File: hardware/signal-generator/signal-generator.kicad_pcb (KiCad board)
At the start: 4 copper layers, 135 parts, among them J1 AVR-ISP-6, J10 Output_Conn, J11 SD_Card_Conn, J12 TP_Conn, J13 LCD_Conn, J2 AVR_SPI, J3 PORT_G, J4 PORT_F, J5 PORT_E, J6 PORT_A, J7 PORT_C, J8 AREF, J9 Power_Supply_Rails, Q1 AP2310GN, Q2 AP2310GN, Q3 AP2310GN, Q4 AP2310GN, Q5 AP2310GN, Q6 AP2310GN, Q7 AP2310GN, Q8 AP2310GN, Q9 AP2310GN, SW1 RESET_BUTTON, U1 74HC04, U10 MCP23017-E/SO, U11 AD9764AR, U12 TS4061AICT-1.25, U13 74HC4040, U14 74HC4040, U15 MCP4651-502E/ST, U16 AZ431AN-A, U17 AD8021ARZ, U18 MCP4551-103E/MS, U19 AD8021ARZ, U2 74HC08, U20 AD8021ARZ, U21 AD8021ARZ, U3 74HC08, U4 74HC30, U5 ATmega2561-16AU, U6 ADP7142AUJZ-5.0, U7 TC1017-3.3VCTTR, U8 DS1085Z-10+, U9 CY7C1021D-10ZSXI, Y1 16MHz

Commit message: [Signal Generator] Restore PCB layout with new symbol annotations
The new components have been loaded in the PCB file.
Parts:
- added C45: 6.8pF, Capacitors_SMD:C_0805_HandSoldering, F.Cu at (217.5, 95.6)
- added C46: 100nF, Capacitors_SMD:C_0805_HandSoldering, F.Cu at (211.9, 101.3)
- added JP2: Always_On_Backlight, Pin_Headers:Pin_Header_Straight_1x02_Pitch2.54mm, F.Cu at (45.2, 174.4)
- added Q10: AP2310GN, TO_SOT_Packages_SMD:SOT-23_Handsoldering, F.Cu at (57.2, 178.9)
- added Q11: AP2310GN, TO_SOT_Packages_SMD:SOT-23_Handsoldering, F.Cu at (43.3, 191.2)
- added Q12: AP2310GN, TO_SOT_Packages_SMD:SOT-23_Handsoldering, F.Cu at (36.8, 195.7)
- added R45: 560R, Resistors_SMD:R_0805_HandSoldering, F.Cu at (69.1, 179.3)
- added R46: 560R, Resistors_SMD:R_0805_HandSoldering, F.Cu at (65.5, 185.1)
- added R47: 1k6, Resistors_SMD:R_0805_HandSoldering, F.Cu at (65.5, 182.2)
- added R48: 1k6, Resistors_SMD:R_0805_HandSoldering, F.Cu at (55.1, 191.3)
- added R49: 1k6, Resistors_SMD:R_0805_HandSoldering, F.Cu at (55.1, 188.4)
- added R50: 1k6, Resistors_SMD:R_0805_HandSoldering, F.Cu at (48.7, 195.8)
- added R51: 910R, Resistors_SMD:R_0805_HandSoldering, F.Cu at (59.8, 185.5)
- added R52: 910R, Resistors_SMD:R_0805_HandSoldering, F.Cu at (69.1, 176.4)
- added R53: 680R, Resistors_SMD:R_0805_HandSoldering, F.Cu at (63.3, 179.3)
- added RV1: 1k, Potentiometers:Potentiometer_Alps_RK163_Single_Vertical, F.Cu at (108.6, 144.9)
- added U22: AD8021ARZ, Housings_SOIC:SOIC-8_3.9x4.9mm_Pitch1.27mm, F.Cu at (196.1, 95.3)
- C32, C35, C39: value 100nF -> 6.8pF
- C33, C37, C40, C43: value 6.8pF -> 100nF
- C34: moved to B.Cu
- JP1: value Always_On_Backlight -> MANUAL_GAIN; footprint Pin_Headers:Pin_Header_Straight_1x02_Pitch2.54mm -> Resistors_SMD:R_0805_HandSoldering
- Q1, Q2, Q3: value AP2310GN -> MMBF5485
- R10: value 15R/1% -> 10R/1%
- R11: value 10R/1% -> 510R/1%; moved to B.Cu
- R12: value 15R/1% -> 510R/1%; moved to B.Cu
- R13: value 10R/1% -> 1k/1%; moved to B.Cu
- R16: value 1k/1% -> 510R
- R17: value 2k/1% -> 1k/1%; moved to B.Cu
- R18: value 2k/1% -> 1k/1%
- R19: value 1k -> 470k
- R20: value 1k/1% -> 470k
- R21: value 2k/1% -> 100R/1%
- R22: value 1k/1% -> 100R/1%
- R23: value 1k/1% -> 2k
- R24: value 2k/1% -> 200R/1%
- R25: value 2k/1% -> 1k
- R26, R27, R28, R30: value 560R -> 1k
- R29: value 560R -> 200R/1%
- R31: value 560R -> 1k/1%
- R32: value 560R -> 680R
- R33: value 560R -> 2k4/1%
- R34: value 560R -> 100R/1%
- R38, R39, R40, R41: value 1k6 -> 560R
- R42, R43: value 910R -> 560R
- R44: value 680R -> 560R
- R7: value 1k -> 15R/1%
- R8: value 1k2 -> 10R/1%
- R9: value 2k/1% -> 15R/1%
- U15: value MCP4651-502E/ST -> MCP4551-103E/MS; footprint Housings_SSOP:TSSOP-14_4.4x5mm_Pitch0.65mm -> Housings_SSOP:MSOP-8_3x3mm_Pitch0.65mm
- U16: value AZ431AN-A -> AD8021ARZ; footprint TO_SOT_Packages_SMD:SOT-23_Handsoldering -> Housings_SOIC:SOIC-8_3.9x4.9mm_Pitch1.27mm
- U18: value MCP4551-103E/MS -> MCP4716; footprint Housings_SSOP:MSOP-8_3x3mm_Pitch0.65mm -> TO_SOT_Packages_SMD:SOT-23-6_Handsoldering
- U20: value AD8021ARZ -> MIC6211; footprint Housings_SOIC:SOIC-8_3.9x4.9mm_Pitch1.27mm -> TO_SOT_Packages_SMD:SOT-23-5_HandSoldering
- U21: value AD8021ARZ -> AZ431AN-A; footprint Housings_SOIC:SOIC-8_3.9x4.9mm_Pitch1.27mm -> TO_SOT_Packages_SMD:SOT-23_Handsoldering
- moved R33 258.7 mm to (206.3, 97.4)
- moved R32 258.3 mm to (215.5, 89.9)
- moved R30 247.1 mm to (206.3, 100.2)
- moved R29 208.6 mm to (149.0, 137.4)
- moved R34 199.3 mm to (146.0, 131.6)
- moved R2 195.0 mm to (60.4, 166.4)
- moved C1 194.8 mm to (73.3, 165.3)
- moved Q1 194.0 mm to (139.9, 132.5)
- moved U5 192.9 mm to (68.9, 139.4)
- moved Q3 191.8 mm to (131.4, 138.9)
- moved C11 191.5 mm to (76.5, 151.5)
- moved U7 190.7 mm to (67.7, 163.4)
- moved C12 190.2 mm to (68.6, 158.2)
- moved C14 190.1 mm to (88.8, 147.4)
- moved U21 189.7 mm to (203.6, 87.9)
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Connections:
- C30 pad 1: Net-(C30-Pad1) -> +5VA
- C31 pad 2: +5VA -> -12VA
- C32 pad 1: AGND -> Net-(C32-Pad1)
- C33 pad 1: Net-(C33-Pad1) -> AGND
- C35 pad 1: +5VA -> Net-(C35-Pad1)
- C35 pad 2: AGND -> -12VA
- C36 pad 1: AGND -> +12VA
- C36 pad 2: -12VA -> AGND
- C37 pad 1: Net-(C37-Pad1) -> +5VA
- C37 pad 2: -12VA -> AGND
- C39 pad 1: +12VA -> Net-(C39-Pad1)
- C39 pad 2: AGND -> -12VA
- C40 pad 1: Net-(C40-Pad1) -> AGND
- C41 pad 1: +12VA -> AGND
- C41 pad 2: AGND -> +12VA
- C42 pad 1: AGND -> +12VA
- C42 pad 2: -12VA -> AGND
- C43 pad 2: -12VA -> AGND
- C44 pad 1: +12VA -> AGND
- C44 pad 2: AGND -> -12VA
- JP1 pad 1: +3V3 -> Net-(JP1-Pad1)
- JP1 pad 2: AGND -> Net-(JP1-Pad2)
- Q1 pad 1: +3V3 -> Net-(JP1-Pad2)
- Q1 pad 2: /TFT LCD Module Interface Block/MISO_3.3 -> AGND
- Q1 pad 3: /MISO -> Net-(Q1-Pad3)
- Q2 pad 1: +3V3 -> Net-(JP1-Pad2)
- Q2 pad 2: /TFT LCD Module Interface Block/SCK_3.3 -> AGND
- Q2 pad 3: /SCK -> Net-(Q1-Pad3)
- Q3 pad 1: +3V3 -> Net-(JP1-Pad2)
- Q3 pad 2: /TFT LCD Module Interface Block/MOSI_3.3 -> AGND
- Q3 pad 3: /MOSI -> Net-(Q1-Pad3)
- Q4 pad 2: /TFT LCD Module Interface Block/LCD_DC\~RS -> /TFT LCD Module Interface Block/MISO_3.3
- Q4 pad 3: /DC\~RS~_LCD -> /MISO
- Q5 pad 2: /TFT LCD Module Interface Block/LCD_~RESET -> /TFT LCD Module Interface Block/SCK_3.3
- Q5 pad 3: /~RESET~_LCD -> /SCK
- Q6 pad 2: /TFT LCD Module Interface Block/LCD_~CS -> /TFT LCD Module Interface Block/MOSI_3.3
- Q6 pad 3: /~CS~_LCD -> /MOSI
- Q7 pad 2: /TFT LCD Module Interface Block/T_IRQ -> /TFT LCD Module Interface Block/LCD_DC\~RS
- Q7 pad 3: /IRQ_T -> /DC\~RS~_LCD
- Q8 pad 2: /TFT LCD Module Interface Block/T_~CS -> /TFT LCD Module Interface Block/LCD_~RESET
- Q8 pad 3: /~CS~_T -> /~RESET~_LCD
- Q9 pad 2: /TFT LCD Module Interface Block/SD_~CS -> /TFT LCD Module Interface Block/LCD_~CS
- Q9 pad 3: /~CS~_SD -> /~CS~_LCD
- R10 pad 1: /Output Circuitry/INB -> Net-(R10-Pad1)
- R10 pad 2: Net-(R10-Pad2) -> AGND
- R11 pad 1: Net-(R10-Pad2) -> Net-(R11-Pad1)
- R11 pad 2: AGND -> /Output Circuitry/INA
- R12 pad 1: /Output Circuitry/INA -> Net-(R12-Pad1)
- R12 pad 2: Net-(R12-Pad2) -> /Output Circuitry/INB
- R13 pad 1: Net-(R12-Pad2) -> Net-(R12-Pad1)
- R14 pad 2: /Output Circuitry/INA -> /OCAL
- R15 pad 1: Net-(R15-Pad1) -> Net-(R14-Pad1)
- R15 pad 2: /Output Circuitry/INB -> Net-(R15-Pad2)
- R16 pad 1: Net-(R15-Pad1) -> Net-(R16-Pad1)
- R17 pad 1: Net-(R17-Pad1) -> Net-(JP1-Pad1)
- R17 pad 2: /OCAL -> Net-(R11-Pad1)
- R18 pad 1: Net-(R17-Pad1) -> Net-(R18-Pad1)
- R18 pad 2: Net-(R18-Pad2) -> Net-(R14-Pad1)
- R19 pad 1: Net-(R19-Pad1) -> Net-(Q1-Pad3)
- R19 pad 2: AGND -> /Output Circuitry/GAINCTRL
- R20 pad 1: /Output Circuitry/VINamp -> Net-(JP1-Pad2)
- R20 pad 2: Net-(R14-Pad1) -> Net-(Q1-Pad3)
- R21 pad 2: Net-(R17-Pad1) -> +5VA
- R22 pad 2: +5VA -> Net-(R18-Pad1)
- R23 pad 1: Net-(R23-Pad1) -> Net-(JP1-Pad1)
- R23 pad 2: Net-(R21-Pad1) -> Net-(JP1-Pad2)
- R24 pad 2: Net-(R23-Pad1) -> Net-(R22-Pad1)
- R25 pad 1: /Output Circuitry/VOUT -> Net-(R25-Pad1)
- R25 pad 2: Net-(R22-Pad1) -> +5VA
- R26 pad 1: +5VD -> Net-(R26-Pad1)
- R26 pad 2: /MISO -> Net-(R26-Pad2)
- R27 pad 1: +5VD -> AGND
- R27 pad 2: /SCK -> Net-(R26-Pad1)
- R28 pad 1: +5VD -> /Output Circuitry/GAINCTRL
- R28 pad 2: /MOSI -> Net-(R25-Pad1)
- R29 pad 1: +3V3 -> /Output Circuitry/VOUT
- R29 pad 2: /TFT LCD Module Interface Block/MISO_3.3 -> Net-(R21-Pad1)
- R30 pad 1: +3V3 -> +5VA
- R30 pad 2: /TFT LCD Module Interface Block/SCK_3.3 -> Net-(C43-Pad1)
- R31 pad 1: +3V3 -> Net-(R31-Pad1)
- R31 pad 2: /TFT LCD Module Interface Block/MOSI_3.3 -> Net-(JP1-Pad2)
- R32 pad 1: +5VD -> Net-(R32-Pad1)
- R32 pad 2: /DC\~RS~_LCD -> Net-(C43-Pad1)
- R33 pad 1: +5VD -> Net-(R33-Pad1)
- R33 pad 2: /~RESET~_LCD -> Net-(R31-Pad1)
- R34 pad 1: +5VD -> /OCAL
- R34 pad 2: /~CS~_LCD -> Net-(R33-Pad1)
- R35 pad 1: +3V3 -> +5VD
- R35 pad 2: /TFT LCD Module Interface Block/LCD_DC\~RS -> /MISO
- R36 pad 1: +3V3 -> +5VD
- R36 pad 2: /TFT LCD Module Interface Block/LCD_~RESET -> /SCK
- R37 pad 1: +3V3 -> +5VD
- R37 pad 2: /TFT LCD Module Interface Block/LCD_~CS -> /MOSI
- R38 pad 1: +5VD -> +3V3
- R38 pad 2: /IRQ_T -> /TFT LCD Module Interface Block/MISO_3.3
- R39 pad 1: +5VD -> +3V3
- R39 pad 2: /~CS~_T -> /TFT LCD Module Interface Block/SCK_3.3
- R40 pad 2: /TFT LCD Module Interface Block/T_IRQ -> /TFT LCD Module Interface Block/MOSI_3.3
- R41 pad 1: +3V3 -> +5VD
- R41 pad 2: /TFT LCD Module Interface Block/T_~CS -> /DC\~RS~_LCD
- R42 pad 2: /~CS~_SD -> /~RESET~_LCD
- R43 pad 1: +3V3 -> +5VD
- R43 pad 2: /TFT LCD Module Interface Block/SD_~CS -> /~CS~_LCD
- R44 pad 1: AGND -> +3V3
- R44 pad 2: /BL_LCD -> /TFT LCD Module Interface Block/LCD_DC\~RS
- R7 pad 1: +5VA -> /Output Circuitry/INB
- R7 pad 2: Net-(C30-Pad1) -> Net-(R7-Pad2)
- R8 pad 1: Net-(R8-Pad1) -> Net-(R7-Pad2)
- R8 pad 2: Net-(C30-Pad1) -> AGND
- R9 pad 1: /OCAL -> /Output Circuitry/INA
- R9 pad 2: Net-(R9-Pad2) -> Net-(R10-Pad1)
- U15 pad 5: Net-(U15-Pad10) -> +5VA
- U15 pad 6: Net-(U15-Pad10) -> Net-(R15-Pad2)
- U15 pad 7: /Output Circuitry/VINamp -> AGND
- U15 pad 8: Net-(R9-Pad2) -> +5VA
- U16 pad 1: Net-(C30-Pad1) -> AGND
- U16 pad 2: Net-(C30-Pad1) -> Net-(R11-Pad1)
- U16 pad 3: AGND -> Net-(R12-Pad1)
- U17 pad 2: Net-(U15-Pad10) -> Net-(R14-Pad1)
- U17 pad 3: Net-(R8-Pad1) -> Net-(R16-Pad1)
- U17 pad 5: Net-(C33-Pad1) -> Net-(C35-Pad1)
- U17 pad 6: /OCAL -> Net-(R18-Pad1)
- U18 pad 1: AGND -> Net-(R26-Pad2)
- U18 pad 2: /SCL -> AGND
- U18 pad 3: /SDA -> +5VA
- U18 pad 4: AGND -> /SDA
- U18 pad 5: +5VA -> /SCL
- U18 pad 6: Net-(R18-Pad2) -> Net-(U18-Pad6)
- U19 pad 2: Net-(R14-Pad1) -> Net-(R21-Pad1)
- U19 pad 3: Net-(R15-Pad1) -> Net-(R22-Pad1)
- U19 pad 5: Net-(C37-Pad1) -> Net-(C39-Pad1)
- U19 pad 6: /Output Circuitry/VINamp -> /Output Circuitry/VOUT
- U2 pad 1: /DDS System/16-bit Counter/Q11 -> Net-(U2-Pad1)
- U2 pad 10: /DDS System/16-bit Counter/Q5 -> /DDS System/16-bit Counter/Q1
- U2 pad 11: /DDS System/16-bit Counter/CP2I3 -> /DDS System/16-bit Counter/CP2I1
- U2 pad 12: /DDS System/16-bit Counter/Q6 -> /DDS System/16-bit Counter/Q2
- U2 pad 13: /DDS System/16-bit Counter/Q7 -> /DDS System/16-bit Counter/Q3
- U2 pad 2: /DDS System/16-bit Counter/Q10 -> Net-(U2-Pad2)
- U2 pad 3: /DDS System/16-bit Counter/CP2I5 -> Net-(U2-Pad3)
- U2 pad 4: /DDS System/16-bit Counter/Q9 -> Net-(U2-Pad4)
- U2 pad 5: /DDS System/16-bit Counter/Q8 -> Net-(U2-Pad5)
- U2 pad 6: /DDS System/16-bit Counter/CP2I4 -> Net-(U2-Pad6)
- U2 pad 8: /DDS System/16-bit Counter/CP2I2 -> /DDS System/16-bit Counter/CP2I0
- U2 pad 9: /DDS System/16-bit Counter/Q4 -> /DDS System/16-bit Counter/Q0
- U20 pad 1: AGND -> /Output Circuitry/GAINCTRL
- U20 pad 2: Net-(R17-Pad1) -> -12VA
- U20 pad 3: Net-(R19-Pad1) -> Net-(R26-Pad1)
- U20 pad 4: -12VA -> Net-(R25-Pad1)
- U20 pad 5: Net-(C40-Pad1) -> +12VA
- U21 pad 1: AGND -> Net-(C43-Pad1)
- U21 pad 2: Net-(R22-Pad1) -> Net-(C43-Pad1)
- U21 pad 3: Net-(R23-Pad1) -> AGND
- U3 pad 1: Net-(U3-Pad1) -> /DDS System/16-bit Counter/Q11
- U3 pad 10: /DDS System/16-bit Counter/Q1 -> /DDS System/16-bit Counter/Q5
- U3 pad 11: /DDS System/16-bit Counter/CP2I1 -> /DDS System/16-bit Counter/CP2I3
- U3 pad 12: /DDS System/16-bit Counter/Q2 -> /DDS System/16-bit Counter/Q6
- U3 pad 13: /DDS System/16-bit Counter/Q3 -> /DDS System/16-bit Counter/Q7
- U3 pad 2: Net-(U3-Pad2) -> /DDS System/16-bit Counter/Q10
- U3 pad 3: Net-(U3-Pad3) -> /DDS System/16-bit Counter/CP2I5
- U3 pad 4: Net-(U3-Pad4) -> /DDS System/16-bit Counter/Q9
- U3 pad 5: Net-(U3-Pad5) -> /DDS System/16-bit Counter/Q8
- U3 pad 6: Net-(U3-Pad6) -> /DDS System/16-bit Counter/CP2I4
- U3 pad 8: /DDS System/16-bit Counter/CP2I0 -> /DDS System/16-bit Counter/CP2I2
- U3 pad 9: /DDS System/16-bit Counter/Q0 -> /DDS System/16-bit Counter/Q4
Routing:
- net AGND: track 60.8 -> 86.7 mm, vias 32 -> 45
- net Net-(R31-Pad1): track 0.00 -> 23.7 mm, vias 0 -> 3
- net Net-(JP1-Pad1): track 0.00 -> 23.6 mm, vias 0 -> 2
- net /Output Circuitry/INB: track 0.00 -> 11.5 mm, vias 0 -> 1
- net /Output Circuitry/INA: track 0.00 -> 11.5 mm, vias 0 -> 1
- net Net-(C43-Pad1): track 0.00 -> 9.32 mm, vias 0 -> 1
- net +12VA: track 0.00 -> 8.45 mm, vias 0 -> 3
- net Net-(R11-Pad1): track 0.00 -> 6.62 mm, vias 0 -> 1
- net Net-(R12-Pad1): track 0.00 -> 6.47 mm, vias 0 -> 1
- net Net-(R32-Pad1): track 0.00 -> 4.65 mm, vias 0 -> 1
- net Net-(R33-Pad1): track 0.00 -> 3.44 mm, vias 0 -> 1
- net Net-(R10-Pad1): track 0.00 -> 2.15 mm
- net Net-(R7-Pad2): track 0.00 -> 2.15 mm
- net +5VA: track 13.3 -> 15.3 mm
- net Net-(C45-Pad1): track 0.00 -> 1.80 mm
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- added copper zone on F.Cu, net -12VA
- added copper zone on F.Cu, net /OCAL
- added copper zone on F.Cu, net Net-(JP1-Pad1)
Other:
- net class Analog HS Signal added: clearance 0.1905, trace_width 0.381, via_dia 0.6, via_drill 0.3
- net class Bypass Cap added: clearance 0.127, trace_width 0.254, via_dia 0.6, via_drill 0.3
- net class Compensation Cap added: clearance 0.127, trace_width 0.508, via_dia 0.8, via_drill 0.4
- net class Digital Supply: clearance 0.1127 -> 0.127
- net class I2C added: clearance 0.127, trace_width 0.1905, via_dia 0.6, via_drill 0.3

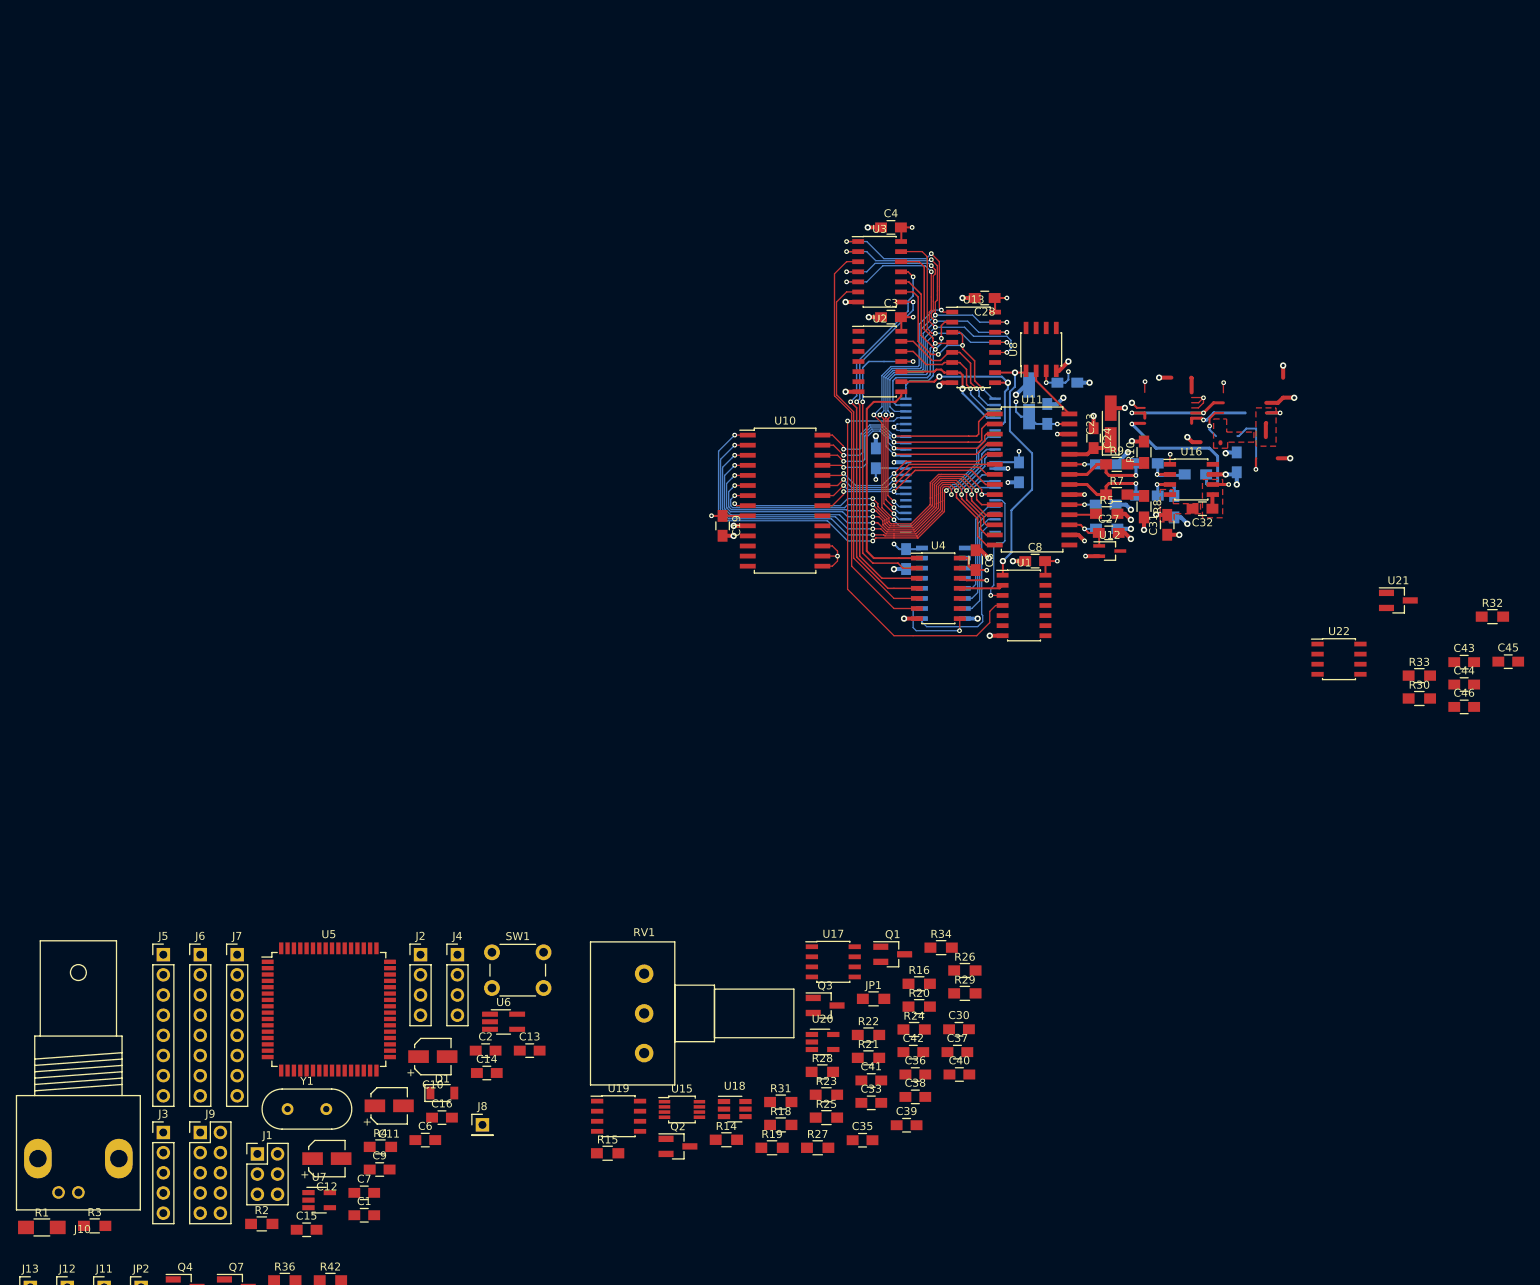
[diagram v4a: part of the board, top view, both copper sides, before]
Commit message: [Signal Generator] Layout output circuitry on PCB
Track lengths are kept to a minimum to facilitate the high-speed
analog signals traversing the output circuitry. As a result the layout
of these components is rather compact.
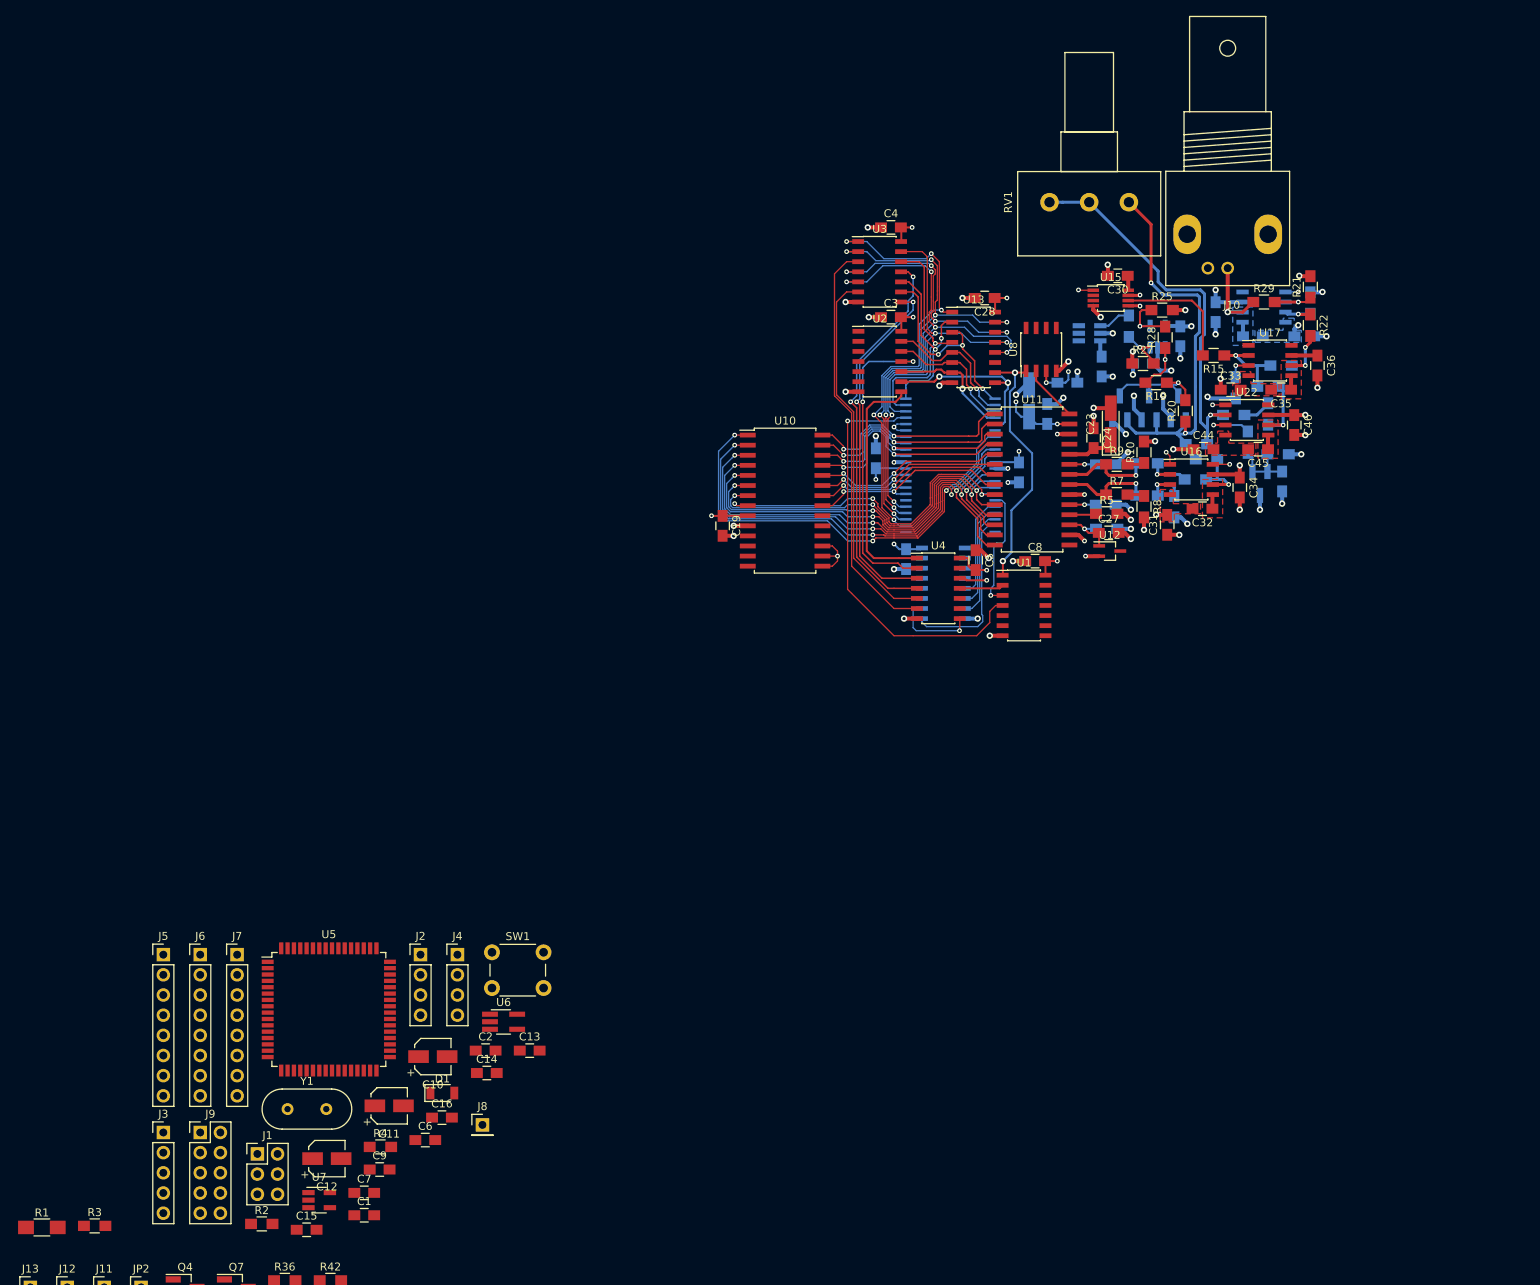
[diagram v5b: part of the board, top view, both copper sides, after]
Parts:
- removed JP1: MANUAL_GAIN, Resistors_SMD:R_0805_HandSoldering
- C34: moved to F.Cu
- C37, C38, C39, C40, C41, C42, C43, Q1, Q2, Q3, R14, R16, R18, R23, R24, R26, R30, R31, R32, R33, R34, U18, U19, U20, U21: moved to B.Cu
- moved J10 185.8 mm to (182.1, 41.0)
- moved U19 130.4 mm to (186.7, 50.9), turned to 180 degrees
- moved R15 126.2 mm to (180.3, 57.0), turned to 180 degrees
- moved RV1 123.4 mm to (169.7, 37.7), turned to 90 degrees
- moved R14 116.9 mm to (187.2, 61.0)
- moved U15 115.6 mm to (167.4, 49.8)
- moved R18 114.6 mm to (188.8, 58.3), turned to 180 degrees
- moved R21 111.9 mm to (192.5, 48.4), turned to 90 degrees
- moved Q2 110.3 mm to (172.2, 63.6), turned to 90 degrees
- moved R25 110.2 mm to (173.9, 51.3)
- moved C39 108.5 mm to (185.3, 54.6)
- moved C35 108.3 mm to (188.8, 61.3), turned to 180 degrees
- moved R19 107.8 mm to (173.1, 60.5), turned to 180 degrees
- moved C38 107.6 mm to (191.8, 54.6), turned to 180 degrees
- moved U18 107.5 mm to (164.7, 54.2), turned to 180 degrees
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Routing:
- net Net-(Q1-Pad1): track 0.00 -> 54.4 mm, vias 0 -> 2
- net AGND: track 86.7 -> 117.4 mm, vias 45 -> 62
- net Net-(R31-Pad1): track 23.7 -> 50.0 mm, vias 3 -> 1
- net Net-(R17-Pad1): track 23.6 -> 7.66 mm, vias 2 -> 1
- net Net-(Q1-Pad3): track 0.00 -> 15.6 mm, vias 0 -> 1
- net Net-(R15-Pad2): track 0.00 -> 15.5 mm
- net +12VA: track 8.45 -> 21.3 mm, vias 3 -> 4
- net /Output Circuitry/VOUT: track 0.00 -> 11.2 mm, vias 0 -> 1
- net Net-(R14-Pad1): track 0.00 -> 10.6 mm, vias 0 -> 1
- net /OCAL: track 0.00 -> 8.85 mm, vias 0 -> 1
- net Net-(R25-Pad1): track 0.00 -> 7.81 mm, vias 0 -> 1
- net Net-(R18-Pad1): track 0.00 -> 7.44 mm, vias 0 -> 2
- net /Output Circuitry/GAINCTRL: track 0.00 -> 7.41 mm, vias 0 -> 1
- net Net-(R26-Pad1): track 0.00 -> 7.11 mm, vias 0 -> 1
- net +5VA: track 15.3 -> 21.8 mm, vias 4 -> 7
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- added copper zone on B.Cu, net -12VA
- added copper zone on B.Cu, net /Output Circuitry/VOUT
- added copper zone on F.Cu, net Net-(R18-Pad1)
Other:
- net class VOUT added: clearance 0.1905, trace_width 0.508, via_dia 0.8, via_drill 0.4

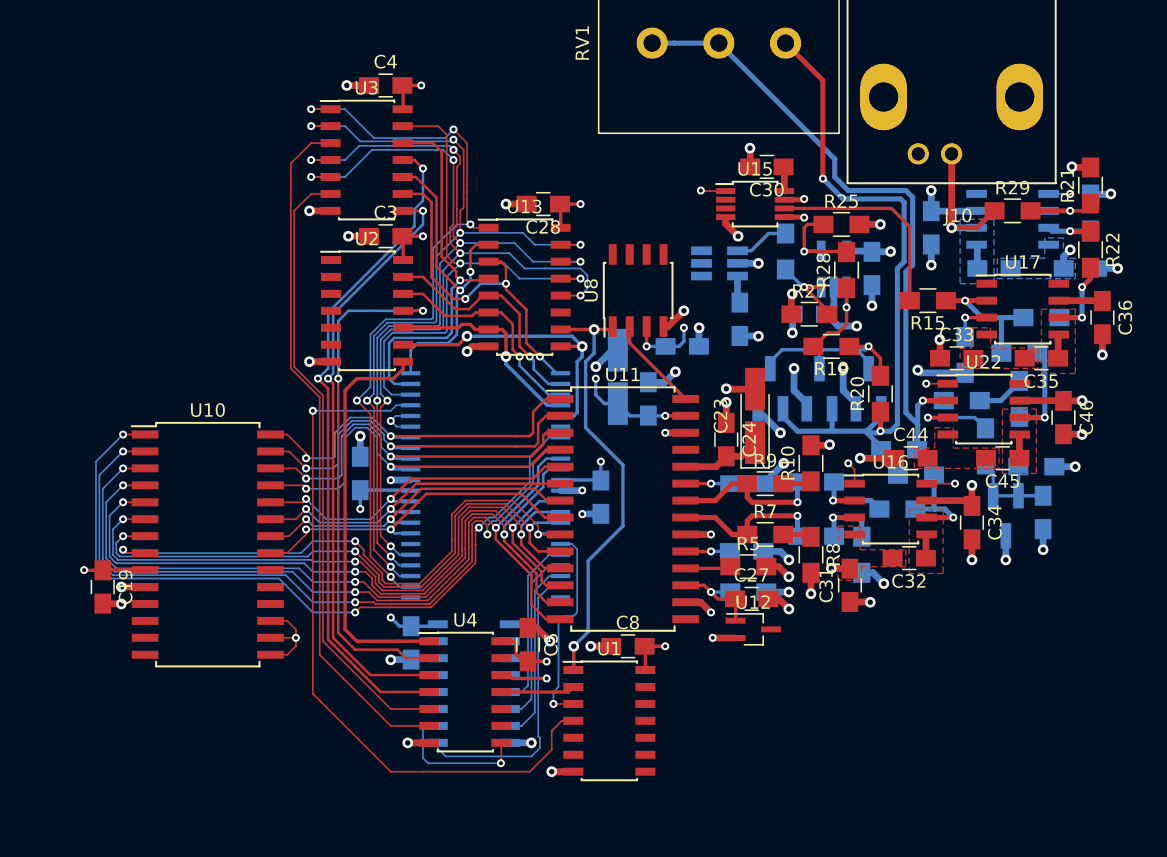
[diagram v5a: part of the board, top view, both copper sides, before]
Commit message: [Signal Generator] Change via dimensions
The via dimensions were previously specified in mm whilst now they are
specified in mils, similar to the track widths. The new dimensions are:
- 0.8mm / 0.4mm -> 32mil / 16mil;
- 0.6mm / 0.3mm -> 24mil / 12mil;
- 20mil / 10mil replace the via which were previously used for digital
signals.
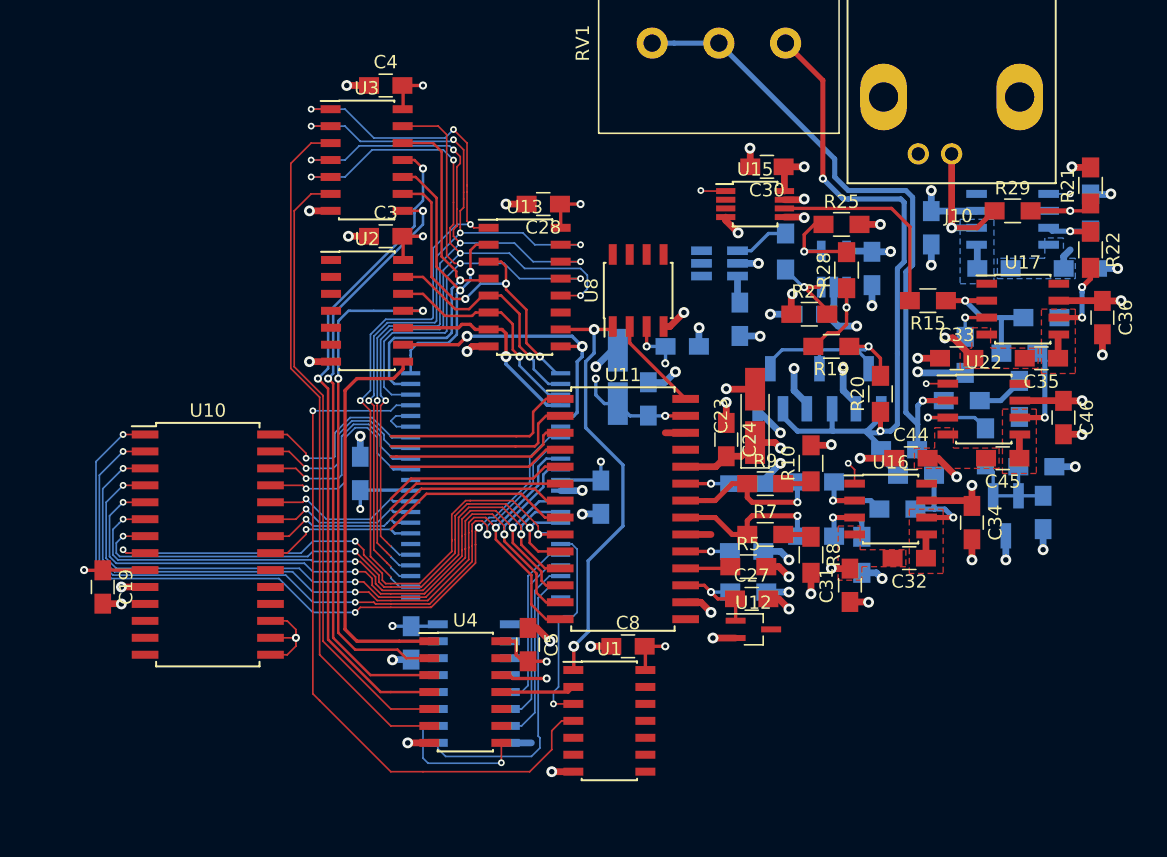
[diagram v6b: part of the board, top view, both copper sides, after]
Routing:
- net -12VA: track 7.96 -> 13.5 mm, vias 3 -> 4
- net +5VA: track 21.8 -> 25.4 mm, vias 7 -> 9
- net /Output Circuitry/~DISABLE: track 2.13 -> 0.00 mm, vias 1 -> 0
- net AGND: track 117.4 -> 115.6 mm, vias 62 -> 57
- net +5VD: track 53.5 -> 52.0 mm
- net +12VA: track 21.3 -> 22.8 mm, vias 4 -> 5
- net /DDS System/16-bit Counter/Q11: track 57.9 -> 57.7 mm, vias 5 -> 4
- net /DDS System/16-bit Counter/Q8: track 63.3 -> 63.2 mm, vias 6 -> 5
- net /DDS System/16-bit Counter/Q10: track 63.5 -> 63.4 mm, vias 6 -> 5
- net Net-(U10-Pad28): vias 2 -> 1
- net Net-(U10-Pad27): vias 2 -> 1
- net Net-(U10-Pad26): vias 2 -> 1
- net Net-(U10-Pad25): vias 2 -> 1
- net Net-(U10-Pad24): vias 2 -> 1
- net Net-(U10-Pad23): vias 2 -> 1
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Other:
- net class Analog HS Signal: via_dia 0.6 -> 0.6096; via_drill 0.3 -> 0.3048
- net class Analog Signal: via_dia 0.6 -> 0.6096; via_drill 0.3 -> 0.3048
- net class Analog Supply: via_dia 0.8 -> 0.8128; via_drill 0.4 -> 0.4064
- net class Bypass Cap: via_dia 0.6 -> 0.6096; via_drill 0.3 -> 0.3048
- net class Compensation Cap: via_dia 0.8 -> 0.8128; via_drill 0.4 -> 0.4064
- net class Digital HS Signal: via_dia 0.6 -> 0.6096; via_drill 0.3 -> 0.3048
- net class Digital Signal: via_dia 0.6 -> 0.508; via_drill 0.3 -> 0.254
- net class Digital Supply: via_dia 0.6 -> 0.6096; via_drill 0.3 -> 0.3048
- net class Digital UHS Signal: via_dia 0.8 -> 0.8128; via_drill 0.4 -> 0.4064
- net class I2C: via_dia 0.6 -> 0.6096; via_drill 0.3 -> 0.3048
- net class VOUT: via_dia 0.8 -> 0.8128; via_drill 0.4 -> 0.4064
